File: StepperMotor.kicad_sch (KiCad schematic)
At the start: 28 parts, among them IC1 MC33926AES, J17 Conn_01x03, J25 Conn_01x03_Pin, J26 Conn_01x03, J27 Conn_01x02, J28 Conn_01x02, J29 Conn_01x02, Q24 MMBT3904WT1G

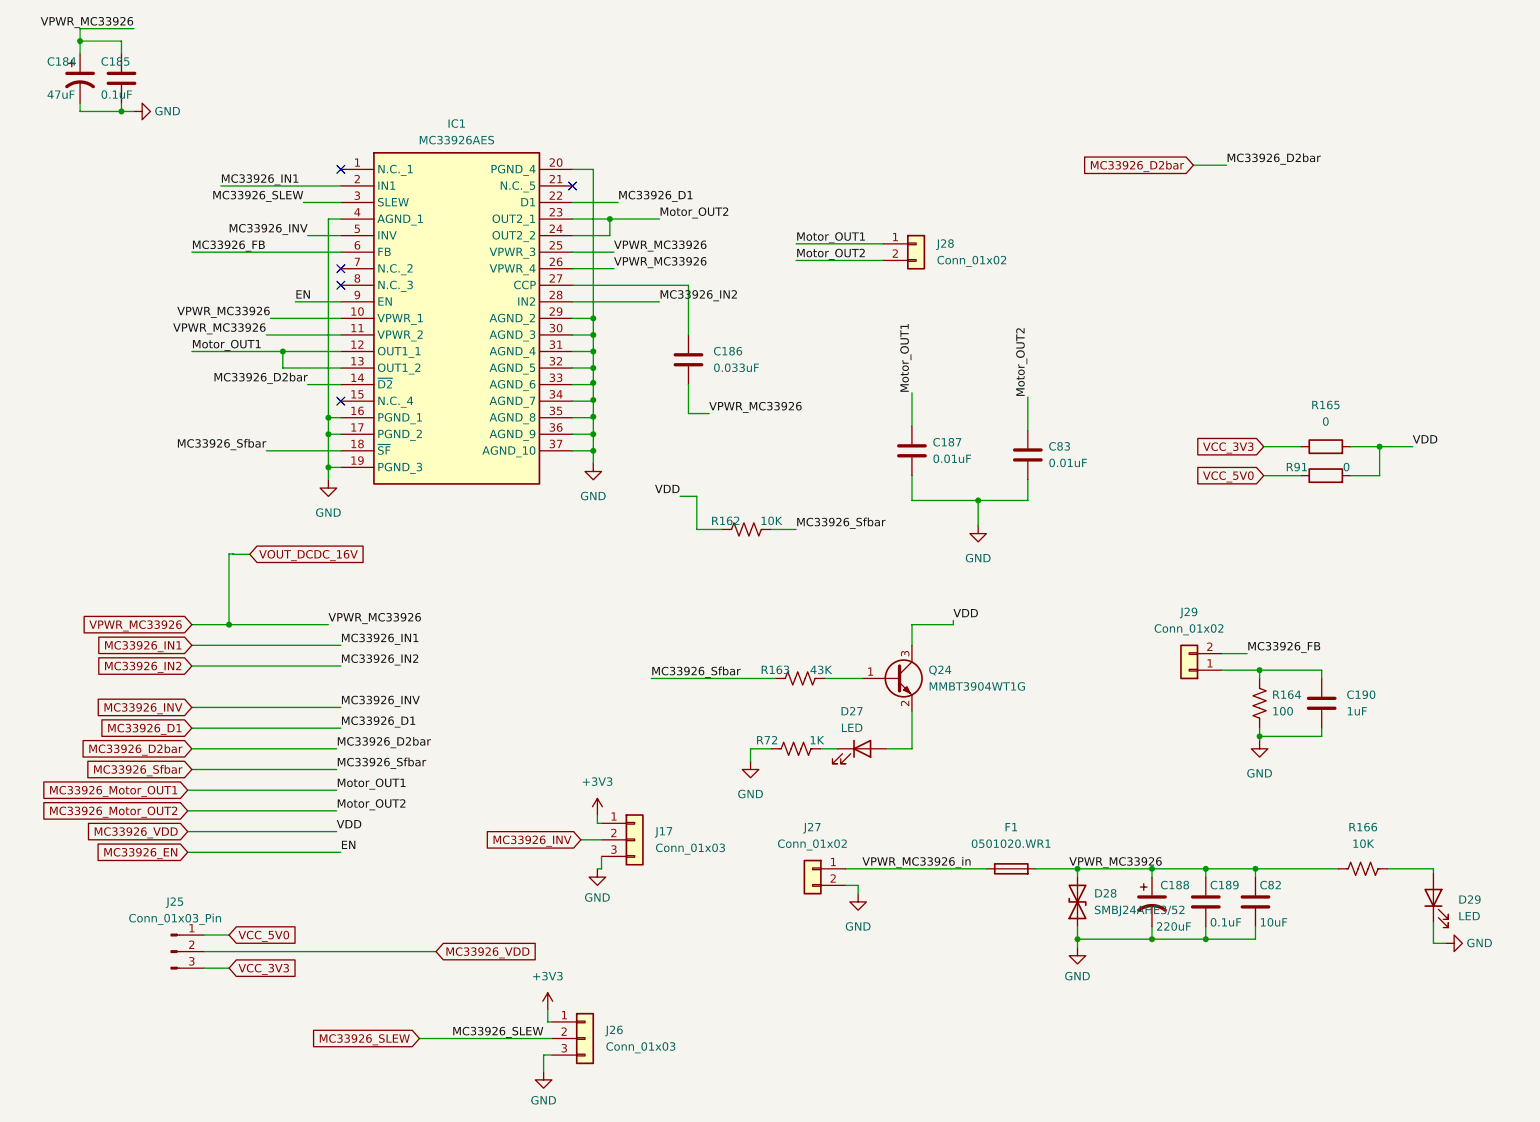
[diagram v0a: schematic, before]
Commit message: add revision to motor
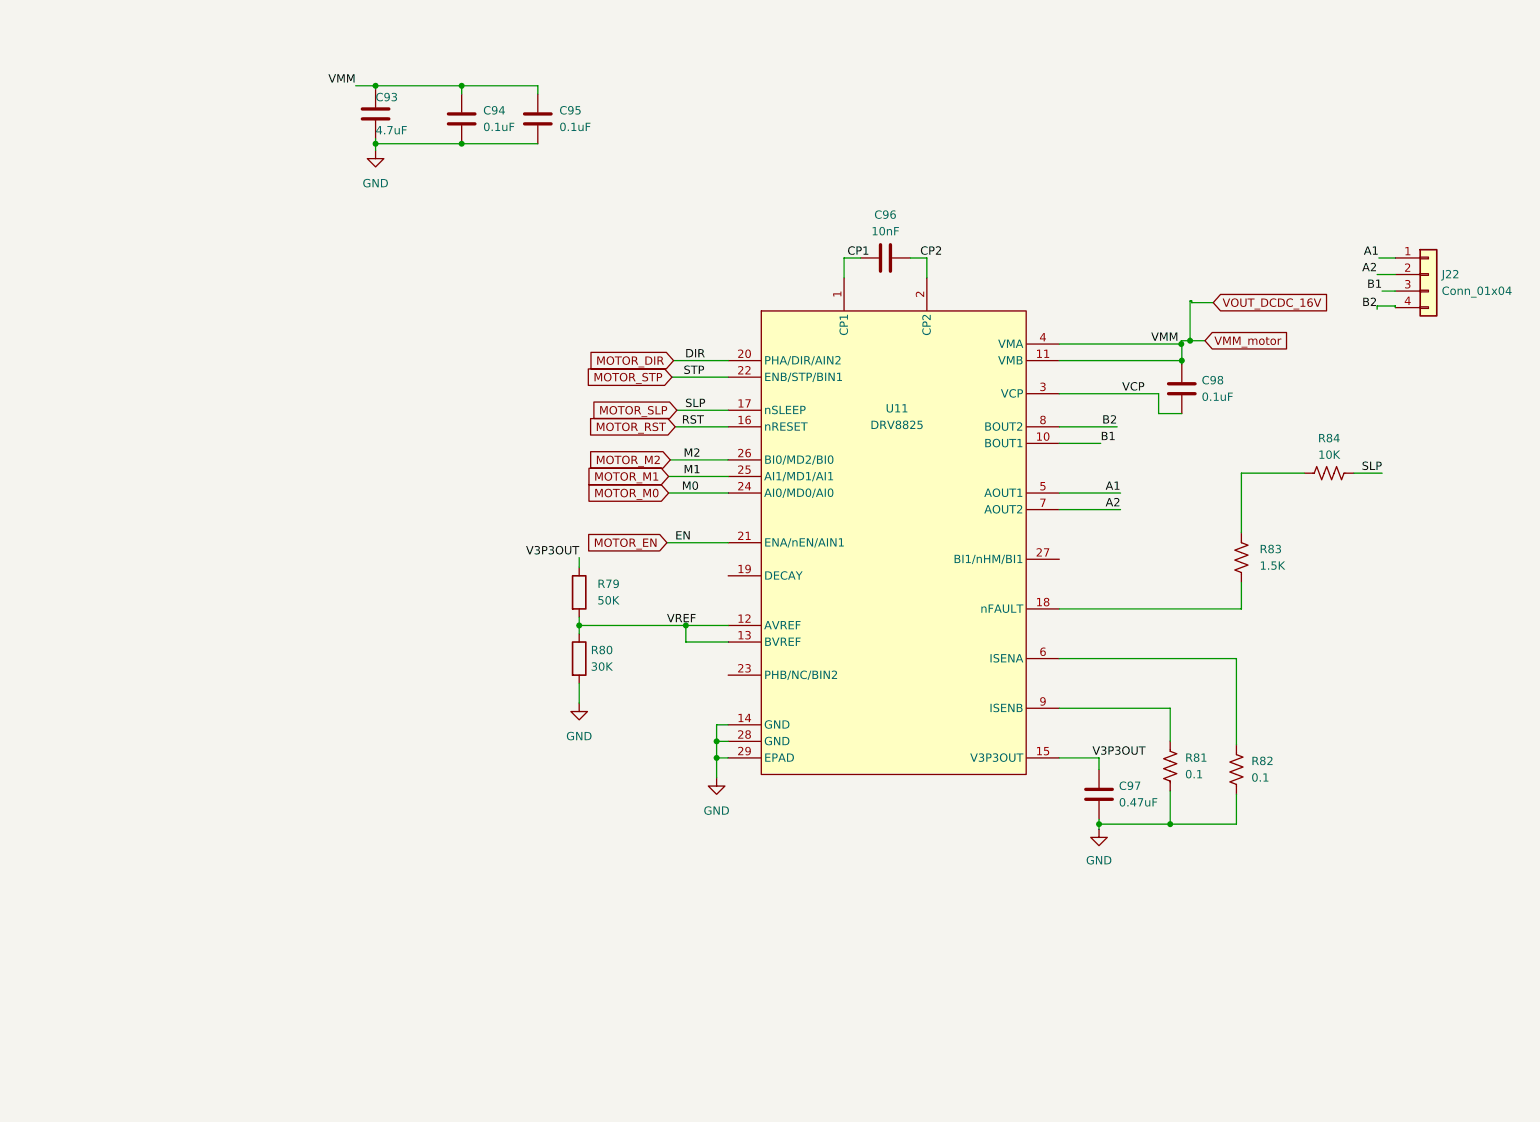
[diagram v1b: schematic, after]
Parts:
- removed C184: 47uF, Capacitor_SMD:C_0603_1608Metric, symbol Device:C_Polarized_US
- removed C185, C189: 0.1uF, Capacitor_SMD:C_0402_1005Metric, symbol Device:C
- removed C186: 0.033uF, Capacitor_SMD:C_0402_1005Metric, symbol Device:C
- removed C187, C83: 0.01uF, Capacitor_SMD:C_0402_1005Metric, symbol Device:C
- removed C188: 220uF, Resistor_SMD:R_0603_1608Metric, symbol Device:C_Polarized_US
- removed C190: 1uF, Capacitor_SMD:C_0402_1005Metric, symbol Device:C
- removed C82: 10uF, Capacitor_SMD:C_0603_1608Metric, symbol Device:C
- removed D27, D29: LED, LED_SMD:LED_0402_1005Metric, symbol Device:LED
- removed D28: SMBJ24AHE3/52, Diode_SMD:D_SMB, symbol Device:D_TVS
- removed F1: 0501020.WR1, Fuse:Fuse_1206_3216Metric, symbol Device:Fuse
- removed IC1: MC33926AES, footprints:MC33926AES, symbol MC33926AES:MC33926AES
- removed J17, J26: Conn_01x03, Connector_PinHeader_2.54mm:PinHeader_1x03_P2.54mm_Vertical, symbol Connector_Generic:Conn_01x03
- removed J25: Conn_01x03_Pin, Connector_PinHeader_2.54mm:PinHeader_1x03_P2.54mm_Vertical, symbol Connector:Conn_01x03_Pin
- removed J27, J28, J29: Conn_01x02, Connector_PinHeader_2.54mm:PinHeader_1x02_P2.54mm_Vertical, symbol Connector_Generic:Conn_01x02
- removed Q24: MMBT3904WT1G, Package_TO_SOT_SMD:SOT-323_SC-70, symbol Transistor_BJT:Q_NPN_BEC
- removed R162, R166: 10K, Resistor_SMD:R_0402_1005Metric, symbol Device:R_US
- removed R163: 43K, Resistor_SMD:R_0402_1005Metric, symbol Device:R_US
- removed R164: 100, Resistor_SMD:R_0402_1005Metric, symbol Device:R_US
- removed R165, R91: 0, Resistor_SMD:R_0402_1005Metric, symbol Device:R
- removed R72: 1K, Resistor_SMD:R_0402_1005Metric, symbol Device:R_US
- added C93: 4.7uF, Capacitor_SMD:C_0402_1005Metric, symbol Device:C
- added C94, C95, C98: 0.1uF, Capacitor_SMD:C_0402_1005Metric, symbol Device:C
- added C96: 10nF, Capacitor_SMD:C_0402_1005Metric, symbol Device:C
- added C97: 0.47uF, Capacitor_SMD:C_0402_1005Metric, symbol Device:C
- added J22: Conn_01x04, Connector_PinSocket_2.54mm:PinSocket_1x04_P2.54mm_Vertical, symbol Connector_Generic:Conn_01x04
- added R79: 50K, Resistor_SMD:R_0402_1005Metric, symbol Device:R
- added R80: 30K, Resistor_SMD:R_0402_1005Metric, symbol Device:R
- added R81, R82: 0.1, Resistor_SMD:R_0402_1005Metric, symbol Device:R_US
- added R83: 1.5K, Resistor_SMD:R_0402_1005Metric, symbol Device:R_US
- added R84: 10K, Resistor_SMD:R_0402_1005Metric, symbol Device:R_US
- added U11: DRV8825, footprints:PWP28_5P18X3P1, symbol qiot:DRV8825
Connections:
- net GND: now also C93.2, C94.2, C95.2, C97.2, R80.2, R81.2, R82.2, U11.14 (GND), U11.28 (GND), U11.29 (EPAD)
- new net: R82.1, U11.6 (ISENA)
- new net: R83.1, R84.1
- new net: R83.2, U11.18 (nFAULT)
- new net: R81.1, U11.9 (ISENB)
- new net A1: J22.1 (Pin_1), U11.5 (AOUT1)
- new net A2: J22.2 (Pin_2), U11.7 (AOUT2)
- new net B1: J22.3 (Pin_3), U11.10 (BOUT1)
- new net B2: J22.4 (Pin_4), U11.8 (BOUT2)
- new net CP1: C96.1, U11.1 (CP1)
- new net CP2: C96.2, U11.2 (CP2)
- new net MOTOR_DIR: U11.20 (PHA/DIR/AIN2)
- new net MOTOR_EN: U11.21 (ENA/nEN/AIN1)
- new net MOTOR_M0: U11.24 (AI0/MD0/AI0)
- new net MOTOR_M1: U11.25 (AI1/MD1/AI1)
- new net MOTOR_M2: U11.26 (BI0/MD2/BI0)
- new net MOTOR_RST: U11.16 (nRESET)
- new net MOTOR_SLP: R84.2, U11.17 (nSLEEP)
- new net MOTOR_STP: U11.22 (ENB/STP/BIN1)
- new net V3P3OUT: C97.1, R79.1, U11.15 (V3P3OUT)
- new net VCP: C98.2, U11.3 (VCP)
- new net VMM_motor: C93.1, C94.1, C95.1, C98.1, U11.11 (VMB), U11.4 (VMA)
- new net VREF: R79.2, R80.1, U11.12 (AVREF), U11.13 (BVREF)
- no-connect marks 5 -> 0

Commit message: del some
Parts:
- renumbered J22 to J23
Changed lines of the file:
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@@
 		(dnp no)
 		(fields_autoplaced yes)
-		(property "Reference" "J22"
+		(property "Reference" "J23"
 			(at 237.49 56.1339 0)
 			(effects
@@
 			(project ""
 				(path "/0db193be-516d-4409-bb62-b8733a9e8874/5d3cc06b-b6bf-4398-9e90-5df16b901332"
-					(reference "J22")
+					(reference "J23")
 					(unit 1)
 				)

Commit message: dad
da
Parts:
- C93: Manufacturer_Part_Number (none) -> CL05A475MP5NRNC
- C94, C95, C98: value 0.1uF -> 100nF; Manufacturer_Part_Number (none) -> CS1005X7R104K500NR
- C96: Manufacturer_Part_Number (none) -> CC0402KRX7R9BB103
- C97: value 0.47uF -> 470nF; Manufacturer_Part_Number (none) -> GRM155R61H474KE11D
- J23: now not fitted
- R79: Manufacturer_Part_Number (none) -> RTT025002FTH
- R80: Manufacturer_Part_Number (none) -> RC0402FR-0730KL
- R81, R82: Manufacturer_Part_Number (none) -> FRL0402JR100TS
- R83: Manufacturer_Part_Number (none) -> 0402WGF1501TCE
- R84: Manufacturer_Part_Number (none) -> RC0402FR-0710KL
- U11: Manufacturer_Part_Number (none) -> DRV8825PWPR
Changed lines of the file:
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@@
 			)
 		)
-		(property "Manufacturer_Part_Number" ""
+		(property "Manufacturer_Part_Number" "FRL0402JR100TS"
 			(at 205.994 132.08 0)
 			(effects
@@
 		)
 		(property "Value2" ""
+			(at 205.994 132.08 0)
+			(effects
+				(font
+					(size 1.27 1.27)
+				)
+			)
+		)
+		(property "partNum" ""
 			(at 205.994 132.08 0)
 			(effects
@@
 			)
 		)
-		(property "Manufacturer_Part_Number" ""
+		(property "Manufacturer_Part_Number" "RC0402FR-0730KL"
 			(at 105.156 115.062 0)
 			(effects
@@
 		)
 		(property "Value2" ""
+			(at 105.156 115.062 0)
+			(effects
+				(font
+					(size 1.27 1.27)
+				)
+			)
+		)
+		(property "partNum" ""
 			(at 105.156 115.062 0)
 			(effects
@@
 			)
 		)
-		(property "Value" "0.47uF"
+		(property "Value" "470nF"
 			(at 187.96 137.1599 0)
 			(effects
@@
 			)
 		)
-		(property "Manufacturer_Part_Number" ""
+		(property "Manufacturer_Part_Number" "GRM155R61H474KE11D"
 			(at 184.912 135.89 0)
 			(effects
@@
 		)
 		(property "Value2" ""
+			(at 184.912 135.89 0)
+			(effects
+				(font
+					(size 1.27 1.27)
+				)
+			)
+		)
+		(property "partNum" ""
 			(at 184.912 135.89 0)
 			(effects
@@
 			)
 		)
-		(property "Value" "0.1uF"
+		(property "Value" "100nF"
 			(at 200.66 74.9299 0)
 			(effects
@@
 			)
 		)
-		(property "Manufacturer_Part_Number" ""
+		(property "Manufacturer_Part_Number" "CS1005X7R104K500NR"
 			(at 197.612 73.66 0)
 			(effects
@@
 		)
 		(property "Value2" ""
+			(at 197.612 73.66 0)
+			(effects
+				(font
+					(size 1.27 1.27)
+				)
+			)
+		)
+		(property "partNum" ""
 			(at 197.612 73.66 0)
 			(effects
@@
 			)
 		)
-		(property "Value" "0.1uF"
+		(property "Value" "100nF"
 			(at 90.424 33.5279 0)
 			(effects
@@
 			)
 		)
-		(property "Manufacturer_Part_Number" ""
+		(property "Manufacturer_Part_Number" "CS1005X7R104K500NR"
 			(at 87.122 32.258 0)
 			(effects
@@
 		)
 		(property "Value2" ""
+			(at 87.122 32.258 0)
+			(effects
+				(font
+					(size 1.27 1.27)
+				)
+			)
+		)
+		(property "partNum" ""
 			(at 87.122 32.258 0)
 			(effects
@@
 			)
 		)
-		(property "Manufacturer_Part_Number" ""
+		(property "Manufacturer_Part_Number" "RC0402FR-0710KL"
 			(at 220.218 86.614 0)
 			(effects
@@
 		)
 		(property "Value2" ""
+			(at 220.218 86.614 0)
+			(effects
+				(font
+					(size 1.27 1.27)
+				)
+			)
+		)
+		(property "partNum" ""
 			(at 220.218 86.614 0)
 			(effects
@@
 			)
 		)
-		(property "Manufacturer_Part_Number" ""
+		(property "Manufacturer_Part_Number" "DRV8825PWPR"
 			(at 153.416 76.962 0)
 			(effects
@@
 		)
 		(property "Value2" ""
+			(at 153.416 76.962 0)
+			(effects
+				(font
+					(size 1.27 1.27)
+				)
+			)
+		)
+		(property "partNum" ""
 			(at 153.416 76.962 0)
 			(effects
@@
 			)
 		)
-		(property "Manufacturer_Part_Number" ""
+		(property "Manufacturer_Part_Number" "CC0402KRX7R9BB103"
 			(at 152.146 53.594 0)
 			(effects
@@
 		)
 		(property "Value2" ""
+			(at 152.146 53.594 0)
+			(effects
+				(font
+					(size 1.27 1.27)
+				)
+			)
+		)
+		(property "partNum" ""
 			(at 152.146 53.594 0)
 			(effects
@@
 			)
 		)
-		(property "Manufacturer_Part_Number" ""
+		(property "Manufacturer_Part_Number" "FRL0402JR100TS"
 			(at 195.834 131.572 0)
 			(effects
@@
 		)
 		(property "Value2" ""
+			(at 195.834 131.572 0)
+			(effects
+				(font
+					(size 1.27 1.27)
+				)
+			)
+		)
+		(property "partNum" ""
 			(at 195.834 131.572 0)
 			(effects
@@
 			)
 		)
-		(property "Manufacturer_Part_Number" ""
+		(property "Manufacturer_Part_Number" "RTT025002FTH"
 			(at 105.156 104.902 0)
 			(effects
@@
 		)
 		(property "Value2" ""
+			(at 105.156 104.902 0)
+			(effects
+				(font
+					(size 1.27 1.27)
+				)
+			)
+		)
+		(property "partNum" ""
 			(at 105.156 104.902 0)
 			(effects
@@
 			)
 		)
-		(property "Manufacturer_Part_Number" ""
+		(property "Manufacturer_Part_Number" "CL05A475MP5NRNC"
 			(at 73.914 31.496 0)
 			(effects
@@
 		)
 		(property "Value2" ""
+			(at 73.914 31.496 0)
+			(effects
+				(font
+					(size 1.27 1.27)
+				)
+			)
+		)
+		(property "partNum" ""
 			(at 73.914 31.496 0)
 			(effects
@@
 			)
 		)
-		(property "Value" "0.1uF"
+		(property "Value" "100nF"
 			(at 102.108 33.5279 0)
 			(effects
@@
 			)
 		)
-		(property "Manufacturer_Part_Number" ""
+		(property "Manufacturer_Part_Number" "CS1005X7R104K500NR"
 			(at 98.806 32.258 0)
 			(effects
@@
 		)
 		(property "Value2" ""
+			(at 98.806 32.258 0)
+			(effects
+				(font
+					(size 1.27 1.27)
+				)
+			)
+		)
+		(property "partNum" ""
 			(at 98.806 32.258 0)
 			(effects
@@
 		(in_bom yes)
 		(on_board yes)
-		(dnp no)
+		(dnp yes)
 		(fields_autoplaced yes)
 		(property "Reference" "J23"
@@
 				)
 				(hide yes)
+			)
+		)
+		(property "partNum" ""
+			(at 235.458 56.134 0)
+			(effects
+				(font
+					(size 1.27 1.27)
+				)
 			)
 		)
@@
 			)
 		)
-		(property "Manufacturer_Part_Number" ""
+		(property "Manufacturer_Part_Number" "0402WGF1501TCE"
 			(at 206.756 99.568 0)
 			(effects
@@
 			(at 206.756 99.568 0)
 			(effects
+				(font
+					(size 1.27 1.27)
+				)
+			)
+		)
+		(property "partNum" ""
+			(at 206.756 99.568 0)
+			(effects

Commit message: gema
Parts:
- C93:  LCSC Part # (none) -> C23733
- C94, C95, C98:  LCSC Part # (none) -> C77020; Manufacturer_Part_Number CS1005X7R104K500NR -> GRM155R71H104KE14D
- C96:  LCSC Part # (none) -> C60133
- C97:  LCSC Part # (none) -> C437527
- R79: footprint Resistor_SMD:R_0402_1005Metric -> Resistor_SMD:R_0603_1608Metric;  LCSC Part # (none) -> C861451; Manufacturer_Part_Number RTT025002FTH -> RT0603BRD0750KL
- R80:  LCSC Part # (none) -> C138008
- R81, R82:  LCSC Part # (none) -> C3013344
- R83:  LCSC Part # (none) -> C25867
- R84:  LCSC Part # (none) -> C60490
- U11:  LCSC Part # (none) -> C81582
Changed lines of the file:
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@@
+			)
+		)
+		(property " LCSC Part #" "C3013344"
+			(at 205.994 132.08 0)
+			(effects
+				(font
+					(size 1.27 1.27)
+				)
+				(hide yes)
 			)
 		)
@@
 			)
 		)
+		(property " LCSC Part #" "C138008"
+			(at 105.156 115.062 0)
+			(effects
+				(font
+					(size 1.27 1.27)
+				)
+				(hide yes)
+			)
+		)
 		(pin "1"
 		)
@@
 			)
 		)
+		(property " LCSC Part #" "C437527"
+			(at 184.912 135.89 0)
+			(effects
+				(font
+					(size 1.27 1.27)
+				)
+				(hide yes)
+			)
+		)
 		(pin "2"
 		)
@@
 			)
 		)
-		(property "Manufacturer_Part_Number" "CS1005X7R104K500NR"
+		(property "Manufacturer_Part_Number" "GRM155R71H104KE14D"
 			(at 197.612 73.66 0)
 			(effects
@@
 					(size 1.27 1.27)
 				)
+			)
+		)
+		(property " LCSC Part #" "C77020"
+			(at 197.612 73.66 0)
+			(effects
+				(font
+					(size 1.27 1.27)
+				)
+				(hide yes)
 			)
 		)
@@
 			)
 		)
-		(property "Manufacturer_Part_Number" "CS1005X7R104K500NR"
+		(property "Manufacturer_Part_Number" "GRM155R71H104KE14D"
 			(at 87.122 32.258 0)
 			(effects
@@
 					(size 1.27 1.27)
 				)
+			)
+		)
+		(property " LCSC Part #" "C77020"
+			(at 87.122 32.258 0)
+			(effects
+				(font
+					(size 1.27 1.27)
+				)
+				(hide yes)
 			)
 		)
@@
 			)
 		)
+		(property " LCSC Part #" "C60490"
+			(at 220.218 86.614 90)
+			(effects
+				(font
+					(size 1.27 1.27)
+				)
+				(hide yes)
+			)
+		)
 		(pin "2"
 		)
@@
 					(size 1.27 1.27)
 				)
+			)
+		)
+		(property " LCSC Part #" "C81582"
+			(at 153.416 76.962 0)
+			(effects
+				(font
+					(size 1.27 1.27)
+				)
+				(hide yes)
 			)
 		)
@@
 			)
 		)
+		(property " LCSC Part #" "C60133"
+			(at 152.146 53.594 90)
+			(effects
+				(font
+					(size 1.27 1.27)
+				)
+				(hide yes)
+			)
+		)
 		(pin "2"
 		)
@@
 			)
 		)
+		(property " LCSC Part #" "C3013344"
+			(at 195.834 131.572 0)
+			(effects
+				(font
+					(size 1.27 1.27)
+				)
+				(hide yes)
+			)
+		)
 		(pin "2"
 		)
@@
 			)
 		)
-		(property "Footprint" "Resistor_SMD:R_0402_1005Metric"
+		(property "Footprint" "Resistor_SMD:R_0603_1608Metric"
 			(at 103.378 104.902 90)
 			(effects
@@
 			)
 		)
-		(property "Manufacturer_Part_Number" "RTT025002FTH"
+		(property "Manufacturer_Part_Number" " RT0603BRD0750KL"
 			(at 105.156 104.902 0)
 			(effects
@@
 					(size 1.27 1.27)
 				)
+			)
+		)
+		(property " LCSC Part #" "C861451"
+			(at 105.156 104.902 0)
+			(effects
+				(font
+					(size 1.27 1.27)
+				)
+				(hide yes)
 			)
 		)
@@
 		)
 		(property "Manufacturer_Part_Number" "CL05A475MP5NRNC"
-			(at 73.914 31.496 0)
+			(at 60.96 34.29 0)
 			(effects
 				(font
@@
 					(size 1.27 1.27)
 				)
+			)
+		)
+		(property " LCSC Part #" "C23733"
+			(at 73.914 31.496 0)
+			(effects
+				(font
+					(size 1.27 1.27)
+				)
+				(hide yes)
 			)
 		)
@@
 			)
 		)
-		(property "Manufacturer_Part_Number" "CS1005X7R104K500NR"
+		(property "Manufacturer_Part_Number" "GRM155R71H104KE14D"
 			(at 98.806 32.258 0)
 			(effects
@@
 					(size 1.27 1.27)
 				)
+			)
+		)
+		(property " LCSC Part #" "C77020"
+			(at 98.806 32.258 0)
+			(effects
+				(font
+					(size 1.27 1.27)
+				)
+				(hide yes)
 			)
 		)
@@
 			)
 		)
+		(property " LCSC Part #" ""
+			(at 235.458 56.134 0)
+			(effects
+				(font
+					(size 1.27 1.27)
+				)
+				(hide yes)
+			)
+		)
 		(pin "3"
 		)
@@
 			)
 		)
+		(property " LCSC Part #" "C25867"
+			(at 206.756 99.568 0)
+			(effects
+				(font
+					(size 1.27 1.27)
+				)
+				(hide yes)
+			)
+		)
